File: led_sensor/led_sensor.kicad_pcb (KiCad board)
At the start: 4 copper layers, 45 parts

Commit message: A
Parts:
- LED0, LED1, LED2, LED3, LED4, LED5, LED6, LED7: footprint LED Lib:XCXZCFBB53W-8VF -> SamacSys_Parts:HSMA-C380
- moved LED7 4.86 mm to (269.1, 135.1), turned to 180 degrees
- moved LED3 4.83 mm to (137.0, 135.1), turned to 180 degrees
- moved LED6 4.83 mm to (236.1, 135.1), turned to 180 degrees
- moved LED5 4.83 mm to (203.1, 135.1), turned to 180 degrees
- moved LED1 4.75 mm to (71.0, 135.1), turned to 180 degrees
- moved LED2 4.75 mm to (104.0, 135.1), turned to 180 degrees
- moved LED4 4.75 mm to (170.1, 135.1), turned to 180 degrees
- moved LED0 4.60 mm to (38.0, 135.1), turned to 180 degrees
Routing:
- net /CCin: track 283.0 -> 274.2 mm
- net /dpin: track 50.0 -> 48.9 mm
- net /din: track 58.8 -> 57.9 mm
- net /gin: track 30.5 -> 29.6 mm
- net /cin: track 36.3 -> 35.5 mm
- net /fin: track 43.1 -> 42.6 mm

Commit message: fixed reverse biased LEDs
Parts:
- moved LED0 8.47 mm to (39.2, 126.7), turned to 0 degrees
- moved LED2 8.33 mm to (105.1, 126.9), turned to 0 degrees
- moved LED4 8.31 mm to (171.0, 126.9), turned to 0 degrees
- moved LED5 8.31 mm to (204.0, 126.9), turned to 0 degrees
- moved LED6 8.30 mm to (236.9, 126.9), turned to 0 degrees
- moved LED3 8.18 mm to (138.0, 127.0), turned to 0 degrees
- moved LED1 8.18 mm to (71.9, 127.0), turned to 0 degrees
- moved LED7 8.06 mm to (270.1, 127.1), turned to 0 degrees
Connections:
- LED0 pad 1: /dpin -> /CCin
- LED0 pad 2: /CCin -> /dpin
- LED1 pad 1: /gin -> /CCin
- LED1 pad 2: /CCin -> /gin
- LED2 pad 1: /fin -> /CCin
- LED2 pad 2: /CCin -> /fin
- LED3 pad 1: /ein -> /CCin
- LED3 pad 2: /CCin -> /ein
- LED4 pad 1: /din -> /CCin
- LED4 pad 2: /CCin -> /din
- LED5 pad 1: /cin -> /CCin
- LED5 pad 2: /CCin -> /cin
- LED6 pad 1: /bin -> /CCin
- LED6 pad 2: /CCin -> /bin
- LED7 pad 1: /ain -> /CCin
- LED7 pad 2: /CCin -> /ain
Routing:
- net /gin: track 29.6 -> 31.0 mm
- net /CCin: track 274.2 -> 273.3 mm
- net /fin: track 42.6 -> 43.3 mm
- net /dpin: track 48.9 -> 49.5 mm

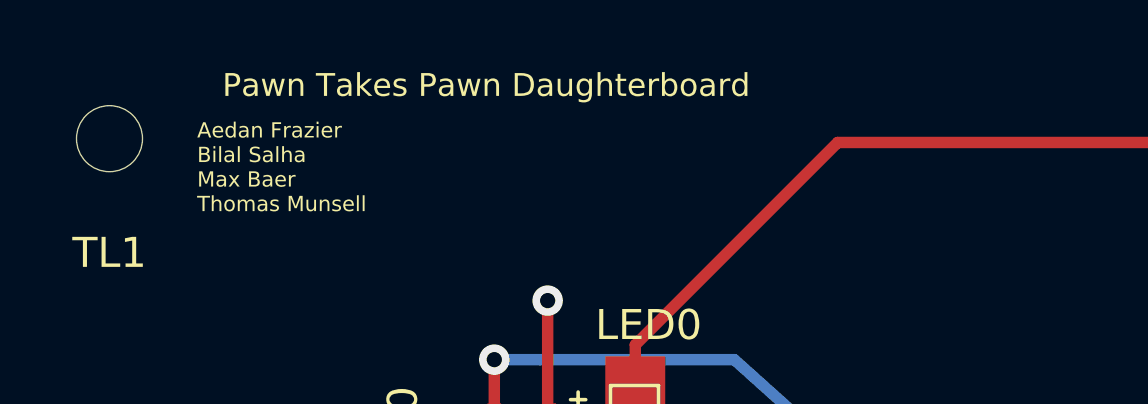
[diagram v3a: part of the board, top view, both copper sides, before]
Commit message: cleaned up directories, silkscreen
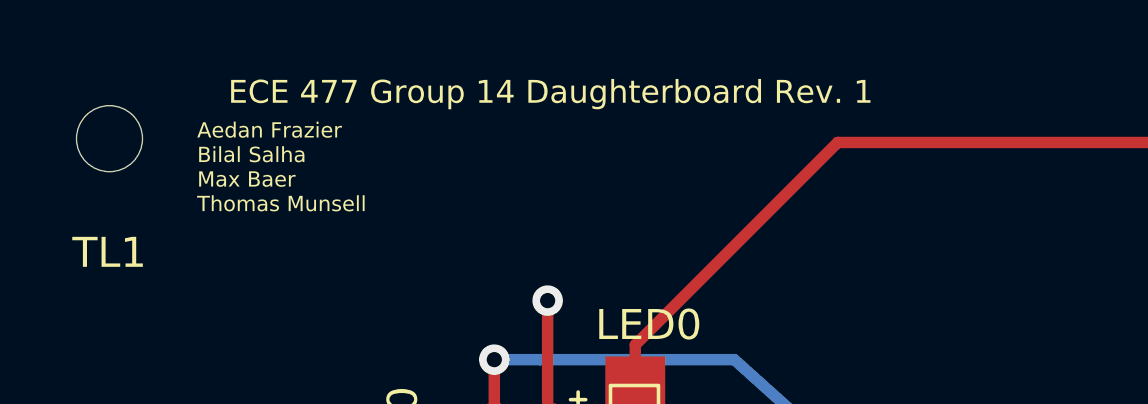
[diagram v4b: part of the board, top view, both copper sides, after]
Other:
- board text added: "ECE 477 Group 14 Daughterboard Rev. 1"
- board text removed: "Pawn Takes Pawn Daughterboard"
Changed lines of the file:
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@@
   )
   (setup
-    (last_trace_width 0.381)
+    (last_trace_width 0.25)
     (user_trace_width 0.2286)
     (user_trace_width 0.381)
@@
     (effects (font (size 0.508 0.508) (thickness 0.127)) (justify left))
   )
-  (gr_text "Pawn Takes Pawn Daughterboard" (at 33.768393 119.253) (layer F.SilkS)
+  (gr_text "ECE 477 Group 14 Daughterboard Rev. 1" (at 35.9156 119.4816) (layer F.SilkS)
     (effects (font (size 0.762 0.762) (thickness 0.1905)))
   )

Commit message: through hole vias
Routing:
- net /gin: track 31.0 -> 28.8 mm
- net +3V3: track 285.3 -> 284.5 mm

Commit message: Reset_Line
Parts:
- added C1: 1u, SamacSys_Parts:CAPC1005X55N, F.Cu at (143.9, 127.7)
- added R1: 10k, SamacSys_Parts:RESC1608X55N, F.Cu at (192.3, 106.8)
- added R2: 10k, SamacSys_Parts:RESC1608X55N, F.Cu at (192.3, 109.4)
- added R3: 10k, SamacSys_Parts:RESC1608X55N, F.Cu at (196.4, 106.8)
- added R4: 10k, SamacSys_Parts:RESC1608X55N, F.Cu at (192.3, 111.9)
- added R5: 10k, SamacSys_Parts:RESC1608X55N, F.Cu at (196.4, 109.4)
- added R6: 10k, SamacSys_Parts:RESC1608X55N, F.Cu at (200.0, 128.7)
- added R7: 10k, SamacSys_Parts:RESC1608X55N, F.Cu at (233.1, 128.3)
- added R8: 10k, SamacSys_Parts:RESC1608X55N, F.Cu at (266.1, 128.6)
- moved LED7 0.88 mm to (270.9, 126.9)
- moved LED6 0.50 mm to (237.4, 126.9)
- moved LED5 0.46 mm to (204.5, 126.9)
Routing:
- net GND: track 336.8 -> 347.1 mm, vias 9 -> 10
- net +3V3: track 284.5 -> 293.4 mm
- net /ain: track 55.5 -> 57.5 mm
- net /CCin: track 273.3 -> 275.0 mm

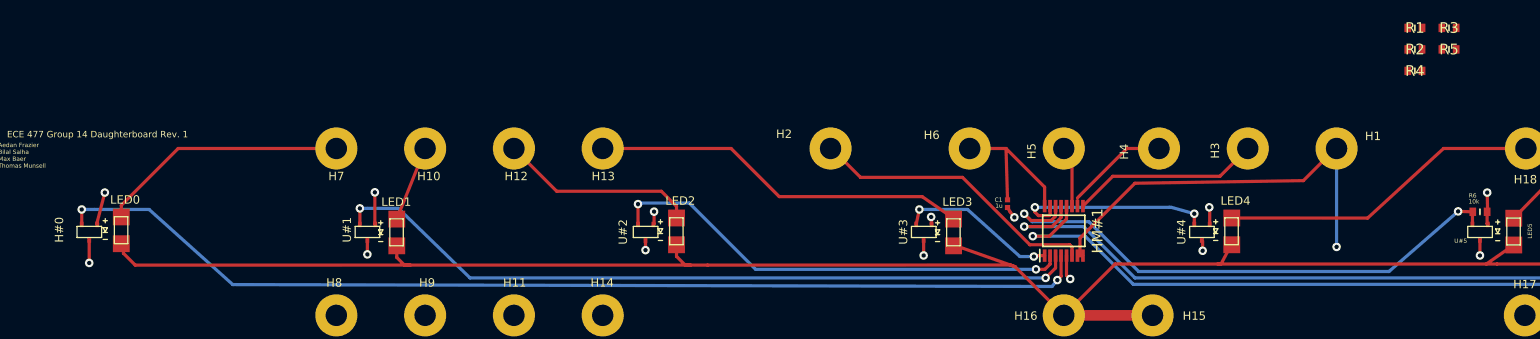
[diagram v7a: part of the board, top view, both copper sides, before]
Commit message: Added Pullups to Daughterboard
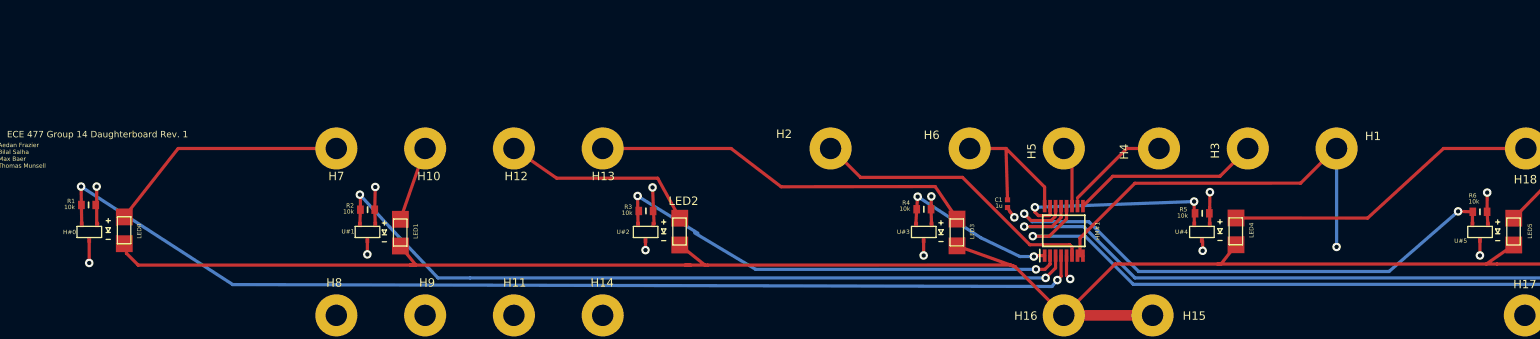
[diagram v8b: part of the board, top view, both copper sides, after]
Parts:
- moved R1 158.9 mm to (34.8, 127.9), turned to 180 degrees
- moved R2 125.8 mm to (68.0, 128.4), turned to 180 degrees
- moved R3 97.8 mm to (101.0, 128.6), turned to 180 degrees
- moved R4 60.6 mm to (134.0, 128.4), turned to 180 degrees
- moved R5 35.2 mm to (167.1, 128.9), turned to 180 degrees
- moved LED4 0.51 mm to (171.5, 126.9)
- moved LED1 0.43 mm to (72.3, 127.0)
- moved LED3 0.41 mm to (138.4, 127.0)
- moved LED2 0.38 mm to (105.5, 126.9)
- moved LED0 0.36 mm to (39.5, 126.7)
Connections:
- R3 pad 1: Net-(R3-Pad1) -> +3V3
- R7 pad 1: Net-(R7-Pad1) -> +3V3
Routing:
- net +3V3: track 293.4 -> 301.3 mm
- net Net-(H#0-Pad3): track 124.5 -> 127.3 mm
- net Net-(HM#1-Pad3): track 90.0 -> 92.6 mm
- net Net-(HM#1-Pad1): track 18.9 -> 20.4 mm
- net Net-(HM#1-Pad15): track 23.9 -> 25.2 mm
- net /CCin: track 275.0 -> 276.1 mm
- net /ein: track 64.6 -> 65.3 mm
- net /din: track 57.9 -> 57.3 mm
- net Net-(HM#1-Pad2): track 55.9 -> 56.4 mm
